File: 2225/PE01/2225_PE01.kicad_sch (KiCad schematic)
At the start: 95 parts, among them J4 Conn_01x01_Male

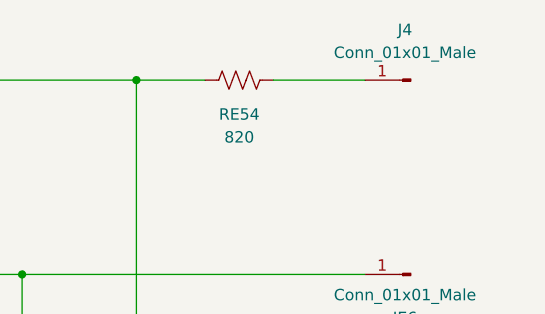
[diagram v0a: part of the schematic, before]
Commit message: Set PCB component positions to match holes on donor board
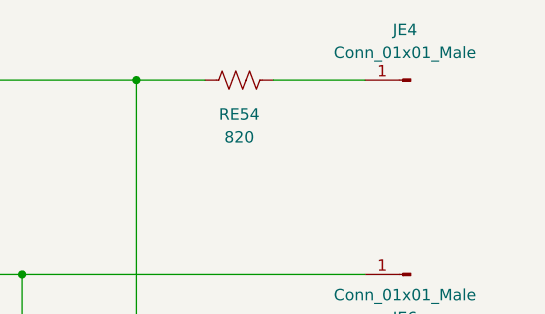
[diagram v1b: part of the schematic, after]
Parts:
- CE23: footprint Capacitor_THT:C_Radial_D6.3mm_H11.0mm_P2.50mm -> Capacitor_THT:C_Radial_D6.3mm_H11.0mm_P3.50mm
- renumbered J4 to JE4
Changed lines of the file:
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@@
     (property "Reference" "CE23" (id 0) (at 405.638 154.178 90))
     (property "Value" "1µF" (id 1) (at 410.718 154.178 90))
-    (property "Footprint" "Capacitor_THT:C_Radial_D6.3mm_H11.0mm_P2.50mm" (id 2) (at 406.908 159.258 0)
+    (property "Footprint" "Capacitor_THT:C_Radial_D6.3mm_H11.0mm_P3.50mm" (id 2) (at 406.908 159.258 0)
       (effects (font (size 1.27 1.27)) hide)
     )
@@
   (symbol (lib_id "Connector:Conn_01x01_Male") (at 483.108 137.668 180) (unit 1)
     (in_bom yes) (on_board yes) (fields_autoplaced)
-    (property "Reference" "J4" (id 0) (at 482.473 132.08 0))
+    (property "Reference" "JE4" (id 0) (at 482.473 132.08 0))
     (property "Value" "Conn_01x01_Male" (id 1) (at 482.473 134.62 0))
     (property "Footprint" "Connector_Pin:Pin_D1.0mm_L10.0mm" (id 2) (at 483.108 137.668 0)
@@
     )
     (path "/23997bb0-e312-4b77-a43a-fe40f4b761fc"
-      (reference "CE23") (unit 1) (value "1µF") (footprint "Capacitor_THT:C_Radial_D6.3mm_H11.0mm_P2.50mm")
+      (reference "CE23") (unit 1) (value "1µF") (footprint "Capacitor_THT:C_Radial_D6.3mm_H11.0mm_P3.50mm")
     )
     (path "/309f1895-3a75-45e3-81d9-c677c6a76a0e"
@@
       (reference "HE8") (unit 1) (value "2SA1015") (footprint "Package_TO_SOT_THT:TO-92_Inline")
     )
-    (path "/ae4741dd-25ac-42b6-92fa-c54eb405c63e"
-      (reference "J4") (unit 1) (value "Conn_01x01_Male") (footprint "Connector_Pin:Pin_D1.0mm_L10.0mm")
-    )
     (path "/863c8908-6d4f-4d21-9d00-9c094e1af9b5"
       (reference "JE1") (unit 1) (value "Conn_01x01_Male") (footprint "Connector_Pin:Pin_D1.0mm_L10.0mm")
@@
       (reference "JE3") (unit 1) (value "Conn_01x01_Male") (footprint "Connector_Pin:Pin_D1.0mm_L10.0mm")
     )
+    (path "/ae4741dd-25ac-42b6-92fa-c54eb405c63e"
+      (reference "JE4") (unit 1) (value "Conn_01x01_Male") (footprint "Connector_Pin:Pin_D1.0mm_L10.0mm")
+    )
     (path "/9a005d17-3056-44bb-9558-cd7583ea6e5b"

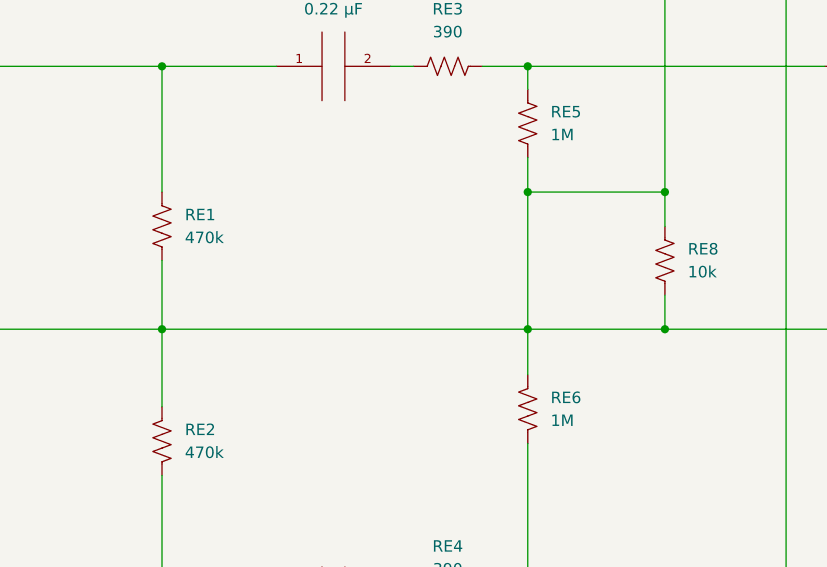
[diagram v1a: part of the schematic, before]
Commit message: Fixed short circuit across RE8. Added traces. Still need ground plane.
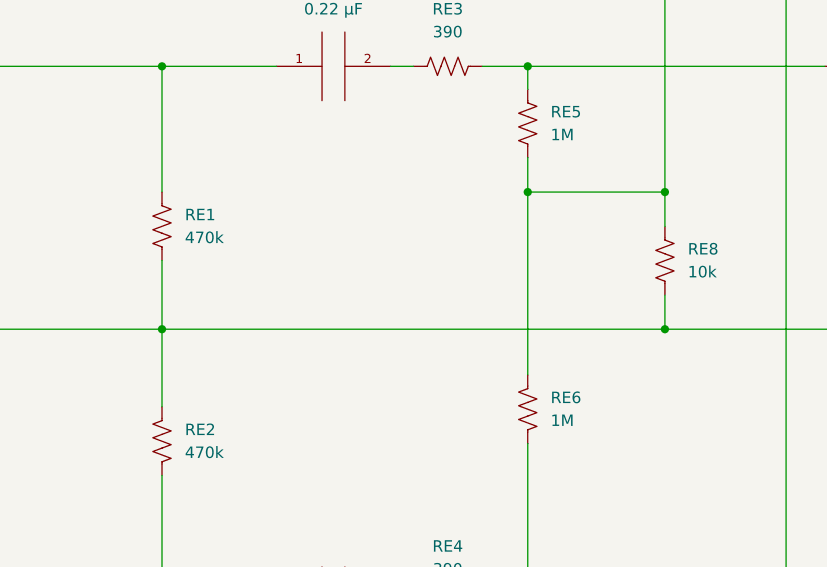
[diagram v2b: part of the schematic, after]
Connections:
- net at CE25.2, CE3.2, CE4.2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: no longer RE5.1, RE6.1, RE7.1, RE8.2
- new net: RE5.1, RE6.1, RE7.1, RE8.2
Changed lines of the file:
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@@
   (junction (at 361.188 180.848) (diameter 0) (color 0 0 0 0)
   )
-  (junction (at 160.528 203.708) (diameter 0) (color 0 0 0 0)
-  )
   (junction (at 319.786 160.528) (diameter 0) (color 0 0 0 0)
   )
@@
     (stroke (width 0) (type default) (color 0 0 0 0))
   )
-  (wire (pts (xy 160.528 208.788) (xy 160.528 203.708))
-    (stroke (width 0) (type default) (color 0 0 0 0))
-  )
   (wire (pts (xy 175.768 137.668) (xy 175.768 146.558))
     (stroke (width 0) (type default) (color 0 0 0 0))
@@
     (stroke (width 0) (type default) (color 0 0 0 0))
   )
-  (wire (pts (xy 160.528 203.708) (xy 175.768 203.708))
+  (wire (pts (xy 119.888 203.708) (xy 175.768 203.708))
     (stroke (width 0) (type default) (color 0 0 0 0))
   )
@@
     (stroke (width 0) (type default) (color 0 0 0 0))
   )
-  (wire (pts (xy 160.528 188.468) (xy 160.528 203.708))
+  (wire (pts (xy 160.528 188.468) (xy 160.528 208.788))
     (stroke (width 0) (type default) (color 0 0 0 0))
   )
@@
     (stroke (width 0) (type default) (color 0 0 0 0))
   )
-  (wire (pts (xy 119.888 203.708) (xy 160.528 203.708))
-    (stroke (width 0) (type default) (color 0 0 0 0))
-  )

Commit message: Updated footprint symbols types to match real board (squiggly resistors, etc). Also updated annotations for RE51, RE52, RE53
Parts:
- RE51: renamed from 100k1; value RE51(HIGH) -> 100k
- RE52: renamed from 100k2; value RE52(MID) -> 100k
- RE53: renamed from 100k3; value RE53(LOW) -> 100k
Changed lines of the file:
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@@
   (symbol (lib_id "Device:Potentiometer_Marantz_RM1014005") (at 332.0189 205.8713 270) (unit 1)
     (in_bom yes) (on_board yes)
-    (property "Reference" "100k3" (id 0) (at 356.1489 203.3313 0)
+    (property "Reference" "RE53" (id 0) (at 356.1489 203.3313 0)
       (effects (font (size 1.27 1.27)) (justify right) hide)
     )
-    (property "Value" "RE53(LOW)" (id 1) (at 328.2089 185.0433 0)
+    (property "Value" "100k" (id 1) (at 328.2089 185.0433 0)
       (effects (font (size 1.27 1.27)) (justify right))
     )
@@
   (symbol (lib_id "Device:Potentiometer_Marantz_RM1014005") (at 274.8689 204.8553 270) (unit 1)
     (in_bom yes) (on_board yes)
-    (property "Reference" "100k1" (id 0) (at 298.9989 202.3153 0)
+    (property "Reference" "RE51" (id 0) (at 298.9989 202.3153 0)
       (effects (font (size 1.27 1.27)) (justify right) hide)
     )
-    (property "Value" "RE51(HIGH)" (id 1) (at 271.0589 184.0273 0)
+    (property "Value" "100k" (id 1) (at 271.0589 184.0273 0)
       (effects (font (size 1.27 1.27)) (justify right))
     )
@@
   (symbol (lib_id "Device:Potentiometer_Marantz_RM1014005") (at 309.1589 204.6013 270) (unit 1)
     (in_bom yes) (on_board yes)
-    (property "Reference" "100k2" (id 0) (at 333.2889 202.0613 0)
+    (property "Reference" "RE52" (id 0) (at 333.2889 202.0613 0)
       (effects (font (size 1.27 1.27)) (justify right) hide)
     )
-    (property "Value" "RE52(MID)" (id 1) (at 305.3489 183.7733 0)
+    (property "Value" "100k" (id 1) (at 305.3489 183.7733 0)
       (effects (font (size 1.27 1.27)) (justify right))
     )
@@
   )
   (symbol_instances
-    (path "/b2dee703-708f-4124-bc6b-2297d7192a37"
-      (reference "100k1") (unit 1) (value "RE51(HIGH)") (footprint "Potentiometer_THT:Potentiometer_Marantz_RM0104005")
-    )
-    (path "/ca6c41eb-69cb-4759-9304-328876274f84"
-      (reference "100k2") (unit 1) (value "RE52(MID)") (footprint "Potentiometer_THT:Potentiometer_Marantz_RM0104005")
-    )
-    (path "/30d333db-7cf9-4c0a-96fe-9f94cdcbf863"
-      (reference "100k3") (unit 1) (value "RE53(LOW)") (footprint "Potentiometer_THT:Potentiometer_Marantz_RM0104005")
-    )
     (path "/46f3b859-597b-4cf4-9608-c0b4fb03231e"
       (reference "CE1") (unit 1) (value "0.22 µF") (footprint "Capacitor_THT:C_Rect_L16.5mm_W4.7mm_P15.00mm_MKT")
@@
       (reference "RE50") (unit 1) (value "470k") (footprint "Resistor_THT:R_Axial_DIN0309_L9.0mm_D3.2mm_P12.70mm_Horizontal")
     )
+    (path "/b2dee703-708f-4124-bc6b-2297d7192a37"
+      (reference "RE51") (unit 1) (value "100k") (footprint "Potentiometer_THT:Potentiometer_Marantz_RM0104005")
+    )
+    (path "/ca6c41eb-69cb-4759-9304-328876274f84"
+      (reference "RE52") (unit 1) (value "100k") (footprint "Potentiometer_THT:Potentiometer_Marantz_RM0104005")
+    )
+    (path "/30d333db-7cf9-4c0a-96fe-9f94cdcbf863"
+      (reference "RE53") (unit 1) (value "100k") (footprint "Potentiometer_THT:Potentiometer_Marantz_RM0104005")
+    )
     (path "/5b2a6257-c31d-4168-a7a6-0301e212888f"

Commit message: Got spice simulation working. Put all component libraries in PE01.lib
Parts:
- added V1, V2: 0, symbol pspice:VSOURCE
- added V3: 35, symbol pspice:VSOURCE
- CE1, CE2: value 0.22 µF -> 0.22u
- CE10, CE9: value 0.22 µF -> 2200p
- CE11, CE12: value 6800pF -> 6800p
- CE13, CE14, CE15, CE16: value 2200pF -> 0.022u
- CE17, CE18: value 0.01µF -> 0.01u
- CE19, CE20, CE23, CE24: value 1µF -> 1u
- CE21, CE22: value 33µF -> 3.3u
- CE25: value 220µF -> 220u
- CE3, CE4: value 10µF -> 10u
- CE5, CE6: value 4.7µF -> 4.7u
- CE7, CE8: value 100pF -> 100p
- HE1, HE2, HE5, HE6: value 2SC1941 -> KSC1845FTA; Spice_Lib_File (none) -> PE01.lib; Spice_Model (none) -> KSC1845; Spice_Netlist_Enabled (none) -> Y; Spice_Node_Sequence (none) -> 2 3 1; Spice_Primitive (none) -> Q
- HE3, HE4, HE7, HE8: value 2SA1015 -> KSA992FTA; Spice_Lib_File (none) -> PE01.lib; Spice_Model (none) -> KSA992; Spice_Netlist_Enabled (none) -> Y; Spice_Node_Sequence (none) -> 2 3 1; Spice_Primitive (none) -> Q
- JE1, JE3, JE4, JE5, JE6, JE7, JE8: Spice_Model (none) -> Conn_01x01_Male; Spice_Netlist_Enabled (none) -> N; Spice_Primitive (none) -> J
- JE2: Spice_Netlist_Enabled (none) -> N; Spice_Primitive (none) -> R
- RE39, RE40: value 2.2M -> 2.2meg
- RE5, RE6: value 1M -> 1meg
- RE51, RE52, RE53: Spice_Lib_File (none) -> PE01.lib; Spice_Model (none) -> POT_LINEAR_2GANG POT_VAL=100k SET=0.5; Spice_Netlist_Enabled (none) -> Y; Spice_Primitive (none) -> X
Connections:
- net GND: now reaches CE25.2, CE3.2, CE4.2, JE3.1 (Pin_1), JE5.1 (Pin_1), JE8.1 (Pin_1), RE1.1, RE11.1, RE12.1, RE17.1, RE18.1, RE2.1, RE41.1, RE42.2, RE47.1, RE48.2, RE49.1, RE50.2, RE8.1
- net GND: now also V1.2 (E2), V2.2 (E2), V3.2 (E2)
- net Vin_L: now reaches CE1.1, JE1.1 (Pin_1), RE1.2
- net Vin_L: now also V2.1 (E1)
- net HE3_E: now reaches CE3.1, HE3.1 (E), RE15.1
- net HE3_C: now reaches CE5.1, HE3.2 (C), RE13.2
- net HE1_C: now reaches HE1.2 (C), HE3.3 (B), RE9.1
- net HE1_B: now reaches HE1.3 (B), RE3.2, RE5.2
- net Vin_R: now reaches CE2.1, JE2.1 (Pin_1), RE2.2
- net Vin_R: now also V1.1 (E1)
- net Vout_L: now reaches CE23.2, JE6.1 (Pin_1), RE49.2
- net HE1_E: now reaches HE1.1 (E), RE11.2, RE13.1
- net Vout_R: now reaches CE24.2, JE7.1 (Pin_1), RE50.1
- net Vcc: now reaches JE4.1 (Pin_1), RE54.2
- net Vcc: now also V3.1 (E1)
- net HE5_B: now reaches CE19.1, HE5.3 (B), RE39.1, RE41.2
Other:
- note added: ".tran 1u 15m"

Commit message: Made board 4 layers and re-routed all the traces.
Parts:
- removed JE1, JE2, JE3, JE4, JE5, JE6, JE7, JE8: Conn_01x01_Male, Connector_Pin:Pin_D1.0mm_L10.0mm, symbol Connector:Conn_01x01_Male
- added J1, J2: Screw_Terminal_01x03, Connector_Molex:Molex_Eurostyle_39357-0003_1x03_P3.5mm_Horizontal, symbol Connector:Screw_Terminal_01x03
- added J3: Screw_Terminal_01x02, Connector_Molex:Molex_Eurostyle_39357-0002_1x02_P3.5mm_Horizontal, symbol Connector:Screw_Terminal_01x02
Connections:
- net GND: now also J1.2 (Pin_2), J2.2 (Pin_2), J3.1 (Pin_1)
- net Vcc: now also J3.2 (Pin_2)
- net Vin_L: now also J1.3 (Pin_3)
- net Vin_R: now also J1.1 (Pin_1)
- net Vout_L: now also J2.1 (Pin_1)
- net Vout_R: now also J2.3 (Pin_3)
- net pwr: now reaches CE25.1, RE10.2, RE15.2, RE16.2, RE39.2, RE40.1, RE45.2, RE46.1, RE54.1, RE7.2, RE9.2

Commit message: Disabled terminal blocks in spice sim of 2225 PE01 because there was no spice model defined for them and the sim wouldnt run
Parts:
- J1, J2: Spice_Model (none) -> Screw_Terminal_01x03; Spice_Netlist_Enabled (none) -> N; Spice_Primitive (none) -> J
- J3: Spice_Model (none) -> Screw_Terminal_01x02; Spice_Netlist_Enabled (none) -> N; Spice_Primitive (none) -> J
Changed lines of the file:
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@@
+      (effects (font (size 1.27 1.27)) hide)
+    )
+    (property "Spice_Primitive" "J" (id 4) (at 81.534 203.708 0)
+      (effects (font (size 1.27 1.27)) hide)
+    )
+    (property "Spice_Model" "Screw_Terminal_01x03" (id 5) (at 81.534 203.708 0)
+      (effects (font (size 1.27 1.27)) hide)
+    )
+    (property "Spice_Netlist_Enabled" "N" (id 6) (at 81.534 203.708 0)
       (effects (font (size 1.27 1.27)) hide)
     )
@@
     )
     (property "Datasheet" "~" (id 3) (at 486.918 203.708 0)
+      (effects (font (size 1.27 1.27)) hide)
+    )
+    (property "Spice_Primitive" "J" (id 4) (at 486.918 203.708 0)
+      (effects (font (size 1.27 1.27)) hide)
+    )
+    (property "Spice_Model" "Screw_Terminal_01x03" (id 5) (at 486.918 203.708 0)
+      (effects (font (size 1.27 1.27)) hide)
+    )
+    (property "Spice_Netlist_Enabled" "N" (id 6) (at 486.918 203.708 0)
       (effects (font (size 1.27 1.27)) hide)
     )
@@
       (effects (font (size 1.27 1.27)) hide)
     )
+    (property "Spice_Primitive" "J" (id 4) (at 478.028 127 0)
+      (effects (font (size 1.27 1.27)) hide)
+    )
+    (property "Spice_Model" "Screw_Terminal_01x02" (id 5) (at 478.028 127 0)
+      (effects (font (size 1.27 1.27)) hide)
+    )
+    (property "Spice_Netlist_Enabled" "N" (id 6) (at 478.028 127 0)
+      (effects (font (size 1.27 1.27)) hide)
+    )

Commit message: Replaced global labels with hierarchical labels, and removed sources and loads, in 2225_PE01.kicad_sch (in prep. for integrating into multi-sheet schematic)
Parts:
- removed V1, V2: 0, symbol pspice:VSOURCE
- removed V3: 35, symbol pspice:VSOURCE
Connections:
- net HE1_C renamed HE3_B
- net Vcc renamed V_power
- net Vin_L renamed V_signal_in_L
- net Vin_R renamed V_signal_in_R

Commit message: Consolidated spice model files (.lib) in models directory. Specified spice paths relative to {KIPRJMOD} env variable.
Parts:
- HE1, HE2, HE3, HE4, HE5, HE6, HE7, HE8, RE51, RE52, RE53: Spice_Lib_File PE01.lib -> ${KIPRJMOD}/../models/PE01/PE01.lib
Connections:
- net V_power renamed V_power_in_35VDC
- net Vout_L renamed V_signal_out_L
- net Vout_R renamed V_signal_out_R
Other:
- note removed: ".tran 1u 15m"
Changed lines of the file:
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@@
     (stroke (width 0) (type default) (color 0 0 0 0))
-  )
-  (text ".tran 1u 15m" (at 57.912 193.548 0)
-    (effects (font (size 1.27 1.27)) (justify left bottom))
   )
   (label "HE1_B" (at 181.102 174.498 0)
@@
     (effects (font (size 1.27 1.27)) (justify left bottom))
   )
-  (hierarchical_label "V_power" (shape input) (at 484.378 137.668 0)
+  (hierarchical_label "V_power_in_35VDC" (shape input) (at 484.378 137.668 0)
     (effects (font (size 1.27 1.27)) (justify left))
   )
@@
     (effects (font (size 1.27 1.27)) (justify right))
   )
-  (hierarchical_label "Vout_L" (shape input) (at 495.808 159.258 0)
+  (hierarchical_label "V_signal_out_L" (shape input) (at 495.808 159.258 0)
     (effects (font (size 1.27 1.27)) (justify left))
   )
@@
     (effects (font (size 1.27 1.27)) (justify right))
   )
-  (hierarchical_label "Vout_R" (shape input) (at 495.808 249.174 0)
+  (hierarchical_label "V_signal_out_R" (shape input) (at 495.808 249.174 0)
     (effects (font (size 1.27 1.27)) (justify left))
   )
@@
       (effects (font (size 1.27 1.27)) hide)
     )
-    (property "Spice_Lib_File" "PE01.lib" (id 7) (at 216.408 165.608 0)
+    (property "Spice_Lib_File" "${KIPRJMOD}/../models/PE01/PE01.lib" (id 7) (at 216.408 165.608 0)
       (effects (font (size 1.27 1.27)) hide)
     )
@@
       (effects (font (size 1.27 1.27)) hide)
     )
-    (property "Spice_Lib_File" "PE01.lib" (id 7) (at 198.628 174.498 0)
+    (property "Spice_Lib_File" "${KIPRJMOD}/../models/PE01/PE01.lib" (id 7) (at 198.628 174.498 0)
       (effects (font (size 1.27 1.27)) hide)
     )
@@
       (effects (font (size 1.27 1.27)) hide)
     )
-    (property "Spice_Lib_File" "PE01.lib" (id 7) (at 406.908 227.584 0)
+    (property "Spice_Lib_File" "${KIPRJMOD}/../models/PE01/PE01.lib" (id 7) (at 406.908 227.584 0)
       (effects (font (size 1.27 1.27)) hide)
     )
@@
       (effects (font (size 1.27 1.27)) hide)
     )
-    (property "Spice_Lib_File" "PE01.lib" (id 7) (at 332.0189 205.8713 0)
+    (property "Spice_Lib_File" "${KIPRJMOD}/../models/PE01/PE01.lib" (id 7) (at 332.0189 205.8713 0)
       (effects (font (size 1.27 1.27)) hide)
     )
@@
       (effects (font (size 1.27 1.27)) hide)
     )
-    (property "Spice_Lib_File" "PE01.lib" (id 7) (at 419.608 236.474 0)
+    (property "Spice_Lib_File" "${KIPRJMOD}/../models/PE01/PE01.lib" (id 7) (at 419.608 236.474 0)
       (effects (font (size 1.27 1.27)) hide)
     )
@@
       (effects (font (size 1.27 1.27)) hide)
     )
-    (property "Spice_Lib_File" "PE01.lib" (id 7) (at 216.408 242.824 0)
+    (property "Spice_Lib_File" "${KIPRJMOD}/../models/PE01/PE01.lib" (id 7) (at 216.408 242.824 0)
       (effects (font (size 1.27 1.27)) hide)
     )
@@
       (effects (font (size 1.27 1.27)) hide)
     )
-    (property "Spice_Lib_File" "PE01.lib" (id 7) (at 419.608 171.958 0)
+    (property "Spice_Lib_File" "${KIPRJMOD}/../models/PE01/PE01.lib" (id 7) (at 419.608 171.958 0)
       (effects (font (size 1.27 1.27)) hide)
     )
@@
       (effects (font (size 1.27 1.27)) hide)
     )
-    (property "Spice_Lib_File" "PE01.lib" (id 7) (at 274.8689 204.8553 0)
+    (property "Spice_Lib_File" "${KIPRJMOD}/../models/PE01/PE01.lib" (id 7) (at 274.8689 204.8553 0)
       (effects (font (size 1.27 1.27)) hide)
     )
@@
       (effects (font (size 1.27 1.27)) hide)
     )
-    (property "Spice_Lib_File" "PE01.lib" (id 7) (at 309.1589 204.6013 0)
+    (property "Spice_Lib_File" "${KIPRJMOD}/../models/PE01/PE01.lib" (id 7) (at 309.1589 204.6013 0)
       (effects (font (size 1.27 1.27)) hide)
     )
@@
       (effects (font (size 1.27 1.27)) hide)
     )
-    (property "Spice_Lib_File" "PE01.lib" (id 7) (at 198.628 233.934 0)
+    (property "Spice_Lib_File" "${KIPRJMOD}/../models/PE01/PE01.lib" (id 7) (at 198.628 233.934 0)
       (effects (font (size 1.27 1.27)) hide)
     )
@@
       (effects (font (size 1.27 1.27)) hide)
     )
-    (property "Spice_Lib_File" "PE01.lib" (id 8) (at 406.908 180.848 0)
+    (property "Spice_Lib_File" "${KIPRJMOD}/../models/PE01/PE01.lib" (id 8) (at 406.908 180.848 0)
       (effects (font (size 1.27 1.27)) hide)
     )
@@
       (reference "#FLG0101") (unit 1) (value "PWR_FLAG") (footprint "")
     )
-    (path "/05b879d1-8aa1-49a2-87e8-9eb76f131906"
-      (reference "#PWR01") (unit 1) (value "GND") (footprint "")
-    )
-    (path "/3ce5d34f-b9a1-48c0-bf05-d0c0166fcf2b"
-      (reference "#PWR02") (unit 1) (value "GND") (footprint "")
-    )
-    (path "/134b56e9-b628-4649-bd21-d2e191debd60"
-      (reference "#PWR03") (unit 1) (value "GND") (footprint "")
-    )
     (path "/0ff1f404-3f7b-497f-8d6a-2e18fec17d01"
       (reference "#PWR04") (unit 1) (value "GND") (footprint "")
@@
       (reference "#PWR0101") (unit 1) (value "GND") (footprint "")
     )
-    (path "/0faa5e11-0259-4d0c-884e-25db78138b53"
-      (reference "#PWR0102") (unit 1) (value "GND") (footprint "")
-    )
-    (path "/baf18cb4-31cc-4672-a92c-96b9d48ac097"
-      (reference "#PWR0103") (unit 1) (value "GND") (footprint "")
-    )
     (path "/46f3b859-597b-4cf4-9608-c0b4fb03231e"
       (reference "CE1") (unit 1) (value "0.22u") (footprint "Capacitor_THT:C_Rect_L16.5mm_W4.7mm_P15.00mm_MKT")
@@
       (reference "RE54") (unit 1) (value "820") (footprint "Resistor_THT:R_Axial_DIN0309_L9.0mm_D3.2mm_P12.70mm_Horizontal")
     )
-    (path "/f46c505c-b0f2-4db8-aa70-02a0796de153"
-      (reference "RLoad_L1") (unit 1) (value "10k") (footprint "Resistor_THT:R_Axial_DIN0309_L9.0mm_D3.2mm_P12.70mm_Horizontal")
-    )
-    (path "/f690db3d-6668-4eb5-a899-fb1ec2df093f"
-      (reference "RLoad_R1") (unit 1) (value "10k") (footprint "Resistor_THT:R_Axial_DIN0309_L9.0mm_D3.2mm_P12.70mm_Horizontal")
-    )
-    (path "/fc77f112-15f9-4ddb-b5b3-93fa7302c927"
-      (reference "V1") (unit 1) (value "0") (footprint "")
-    )
-    (path "/f8a567d0-8b40-479a-b893-bb34dba39068"
-      (reference "V2") (unit 1) (value "0") (footprint "")
-    )
-    (path "/034a2962-e763-4d34-ab66-570da6a4f0ae"
-      (reference "V3") (unit 1) (value "35") (footprint "")
-    )
-  )
+  )
